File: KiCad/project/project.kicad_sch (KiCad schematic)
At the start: 27 parts, among them P1 TerminalBlock 5P 5.0mm, U1 DRV8313PWPR

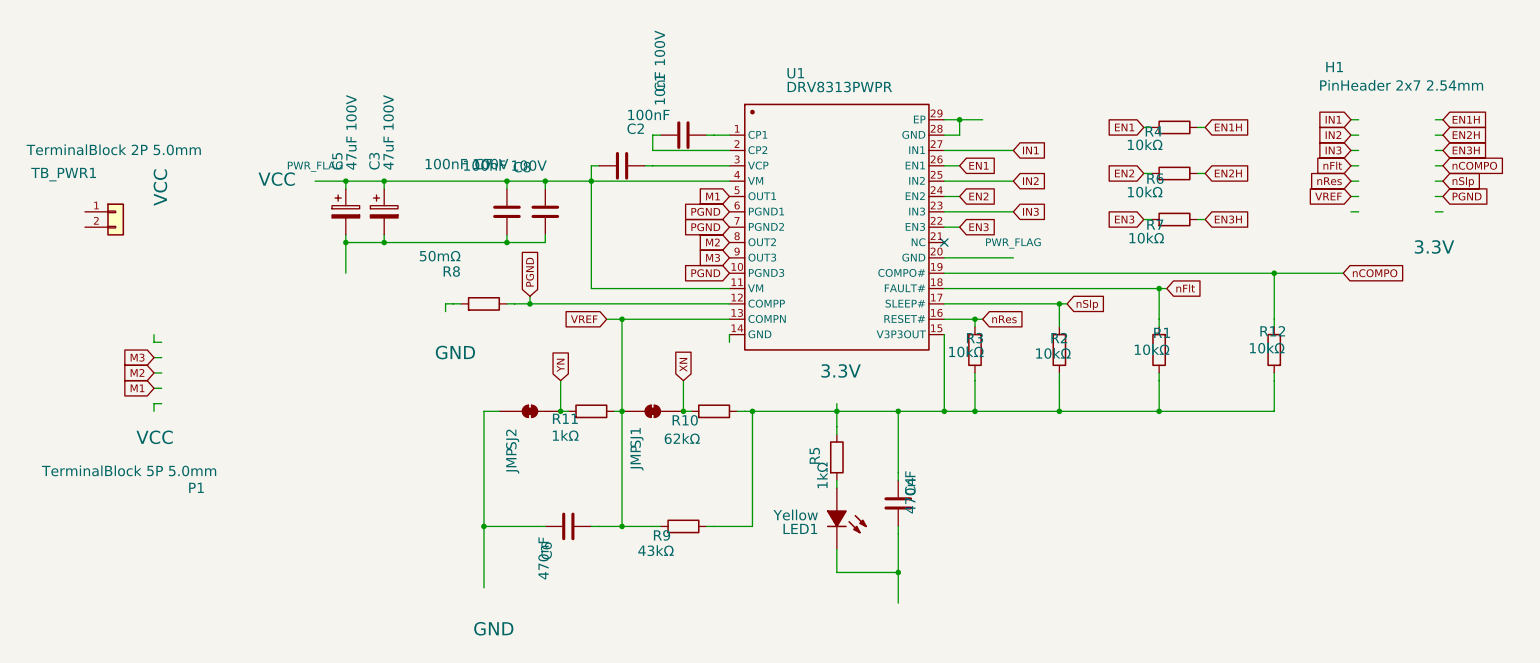
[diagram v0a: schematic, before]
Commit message: Rework
Remove resistors on enable lines.
Redo board layout with clearer and wider power paths.
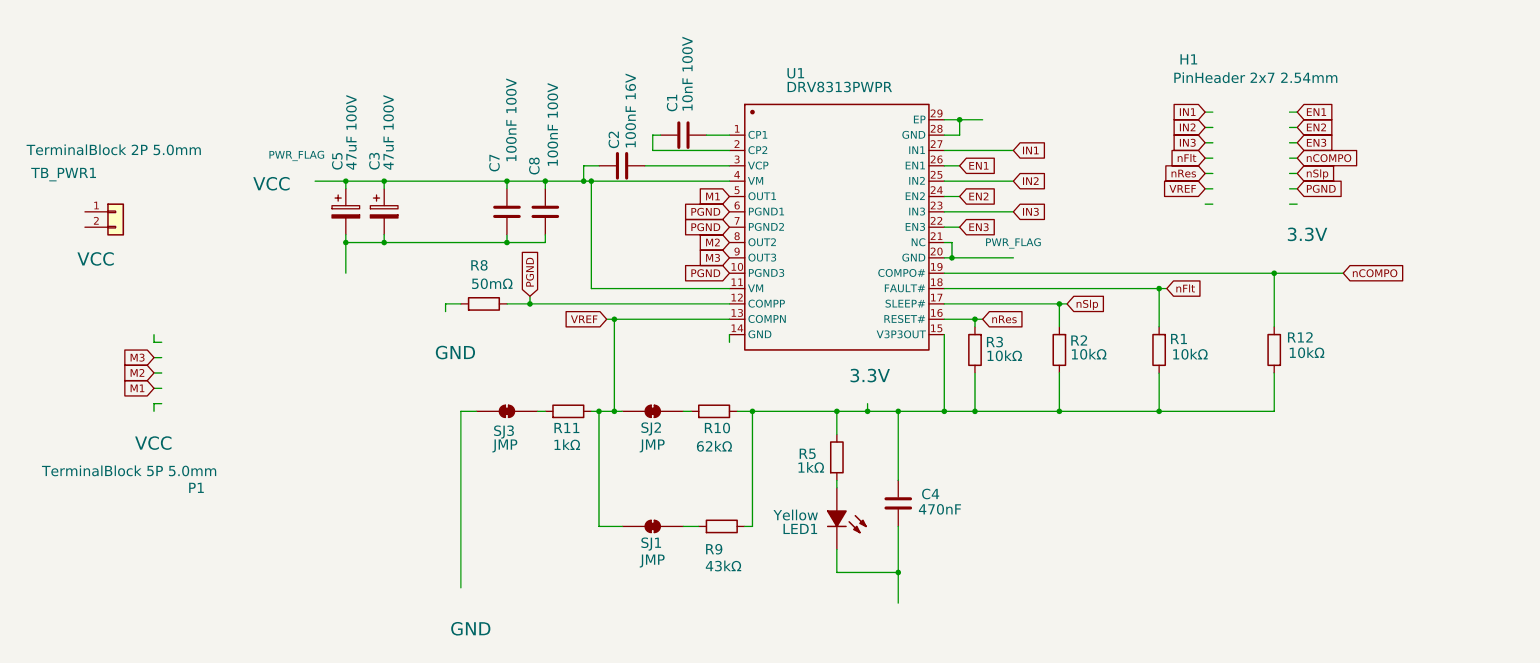
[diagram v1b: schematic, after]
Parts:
- removed C6: 470nF, drv8313-board:C0603, symbol Device:C
- removed R4, R6, R7: 10kΩ, drv8313-board:R0603, symbol Device:R
- added SJ1: JMP, Jumper:SolderJumper-2_P1.3mm_Bridged_RoundedPad1.0x1.5mm, symbol Jumper:SolderJumper_2_Bridged
- C2: value 100nF -> 100nF 16V
- renumbered SJ1 to SJ2, SJ2 to SJ3
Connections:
- net VREF: now also SJ1.2 (B); no longer R9.2
- net at U1.20 (GND): now also U1.21 (NC)
- net XN: no longer names the net of R10.2, SJ2.1 (A)
- net YN: no longer names the net of R11.2, SJ3.1 (A)
- new net: R9.2, SJ1.1 (A)
- no-connect marks 1 -> 0
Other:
- moved on the sheet: R11, R12, R9, SJ2, SJ3

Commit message: Further refinements.
Restore GND symbols.
Note 3V3 max output.
Add logic table for current limit divider.
Add EN1-2/2-3 solder jumpers.
Add VIAs near GND pins.
Route pin 12 comparator input from R8.
Copper keep-out around mounting holes.
Rotate C3 so it's more in the return path from P1.
Add QR code.
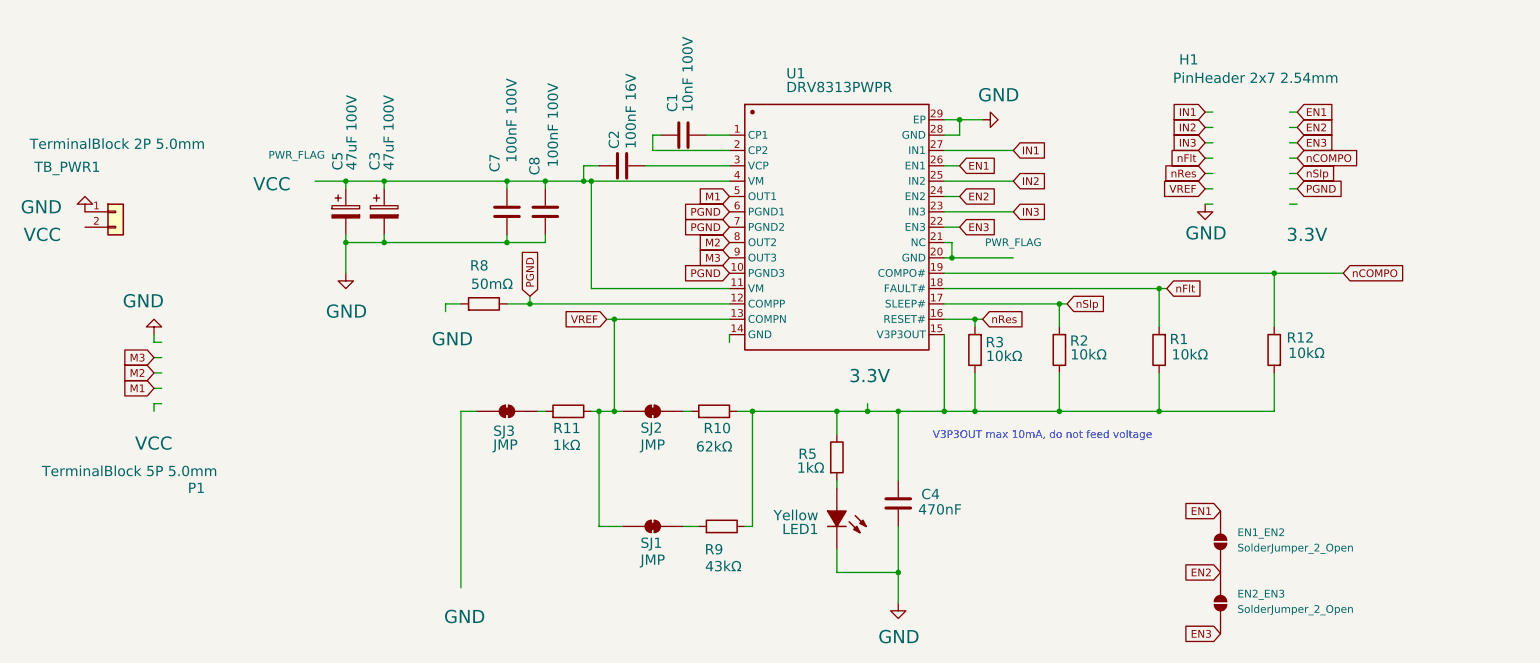
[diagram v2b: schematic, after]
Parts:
- added EN1_EN2, EN2_EN3: SolderJumper_2_Open, Jumper:SolderJumper-2_P1.3mm_Open_RoundedPad1.0x1.5mm, symbol Jumper:SolderJumper_2_Open
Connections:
- net EN1: now also EN1_EN2.1 (A)
- net EN2: now also EN1_EN2.2 (B), EN2_EN3.1 (A)
- net EN3: now also EN2_EN3.2 (B)
- net GND: now reaches C3.2, C5.2, C7.1, C8.1
- net GND: now also C4.1, LED1.2 (C), TB_PWR1.1 (Pin_1), U1.28 (GND), U1.29 (EP)
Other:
- note added: "V3P3OUT max 10mA, do not feed voltage"
